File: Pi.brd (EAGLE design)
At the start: 160 x 100 mm, 14 parts, among them IC1 DS18B20, X1 RASPI_GPIO_B+#_PIN, X2 HDD, 5V 700mA, X3 MAC64L

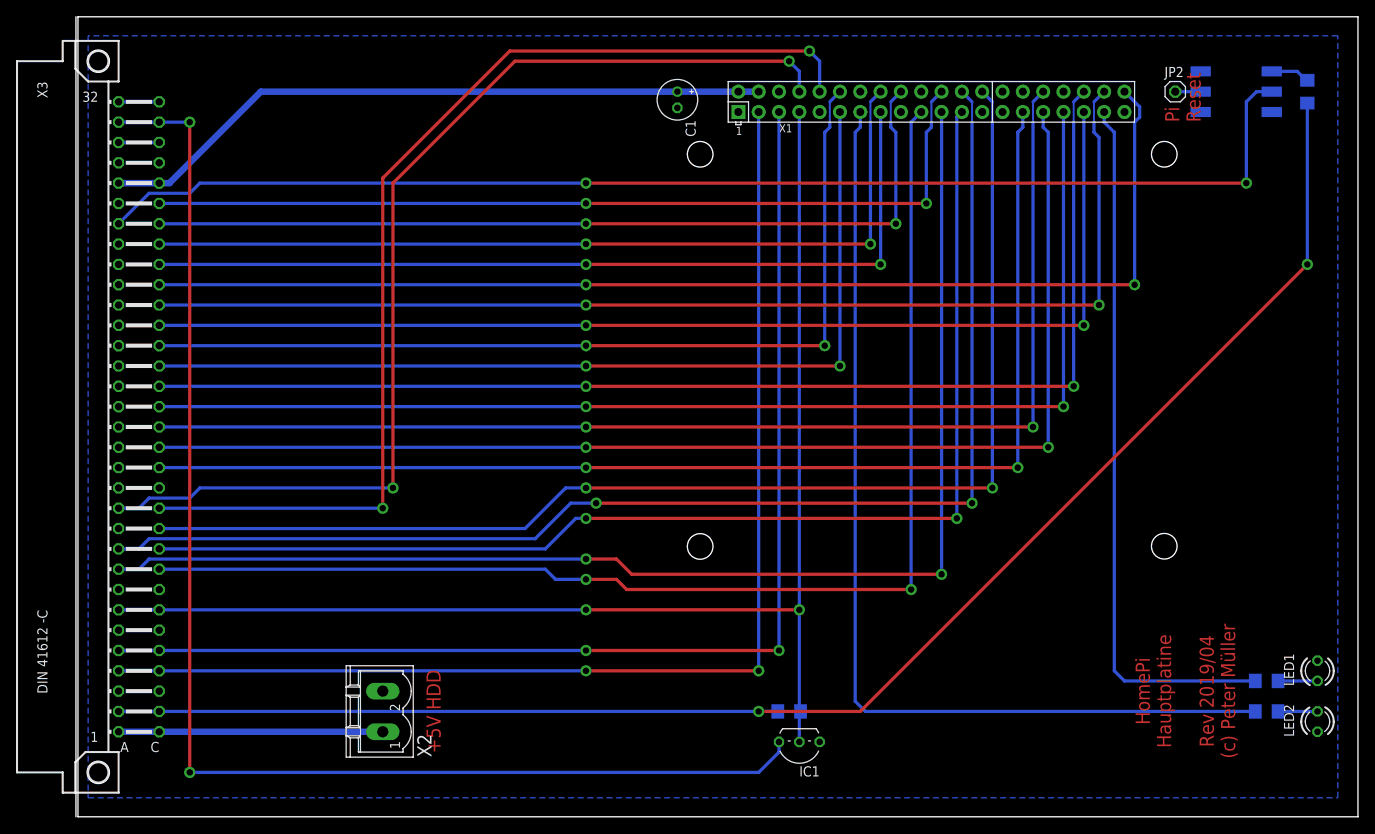
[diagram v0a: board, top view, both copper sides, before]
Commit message: Pi-Display hinzugefügt, Boards angepasst
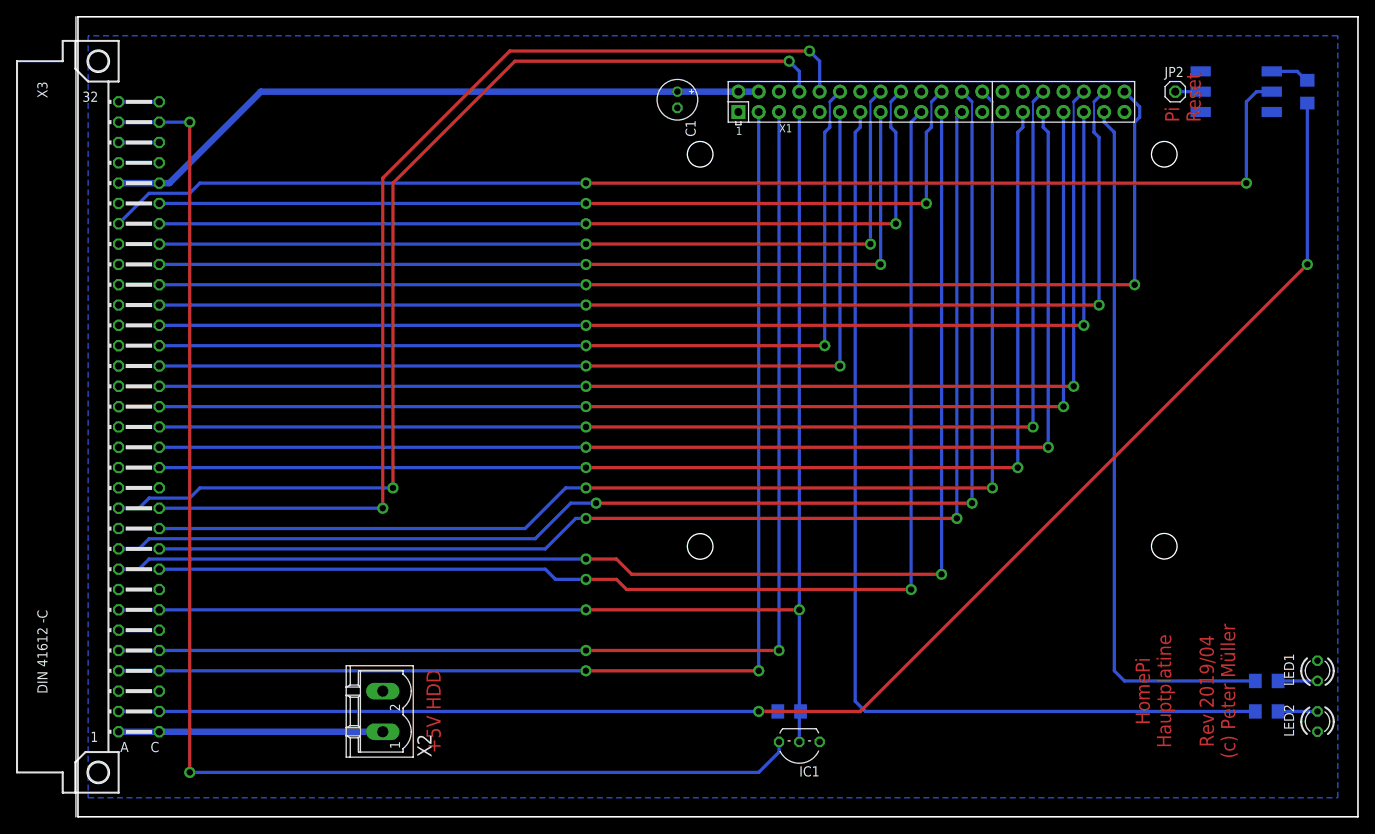
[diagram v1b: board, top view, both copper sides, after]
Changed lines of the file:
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@@
 <board>
 <plain>
-<wire x1="0" y1="-0.47" x2="160" y2="-0.47" width="0" layer="20"/>
-<wire x1="160" y1="-0.47" x2="160" y2="99.53" width="0" layer="20"/>
-<wire x1="160" y1="99.53" x2="0" y2="99.53" width="0" layer="20"/>
-<wire x1="0" y1="99.53" x2="0" y2="-0.47" width="0" layer="20"/>
+<wire x1="0" y1="-0.47" x2="160" y2="-0.47" width="0.2" layer="20"/>
+<wire x1="160" y1="-0.47" x2="160" y2="99.53" width="0.2" layer="20"/>
+<wire x1="160" y1="99.53" x2="0" y2="99.53" width="0.2" layer="20"/>
+<wire x1="0" y1="99.53" x2="0" y2="-0.47" width="0.2" layer="20"/>
 <text x="138.43" y="15.24" size="1.778" layer="1" font="vector" ratio="15" rot="R270" align="center">HomePi
 Hauptplatine
